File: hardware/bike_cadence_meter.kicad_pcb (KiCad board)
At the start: 2 copper layers, 43.5 x 29 mm, 16 parts, among them J1 3034, J2 1x04, SW1 SW_Push, U2 LSM6DS3, Y1 CM130_9pf_+-20ppm

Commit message: Add manufacturing files
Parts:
- added GND: TestPoint, TestPoint:TestPoint_Pad_D1.0mm, F.Cu at (36.2, 43.8)
- added P13: TestPoint, TestPoint:TestPoint_Pad_D1.0mm, F.Cu at (51.8, 36.2)
- added TP4: TestPoint, TestPoint:TestPoint_Pad_D1.0mm, F.Cu at (57.2, 30.8)
- added VCC: TestPoint, TestPoint:TestPoint_Pad_D1.0mm, F.Cu at (26.5, 43.8)
- moved J2 0.79 mm to (28.6, 46.8)
- moved C1 0.24 mm to (51.0, 28.0)
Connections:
- U1 pad 13: unconnected-(U1-I/O-Pad13) -> Net-(TP1-Pad1)
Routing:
- net Net-(TP1-Pad1): track 0.00 -> 3.81 mm
- net GND: track 55.0 -> 56.3 mm
- net VCC: track 108.6 -> 109.3 mm
- net SWDIO: track 25.6 -> 26.1 mm
- net SWDCLK: track 23.9 -> 24.5 mm

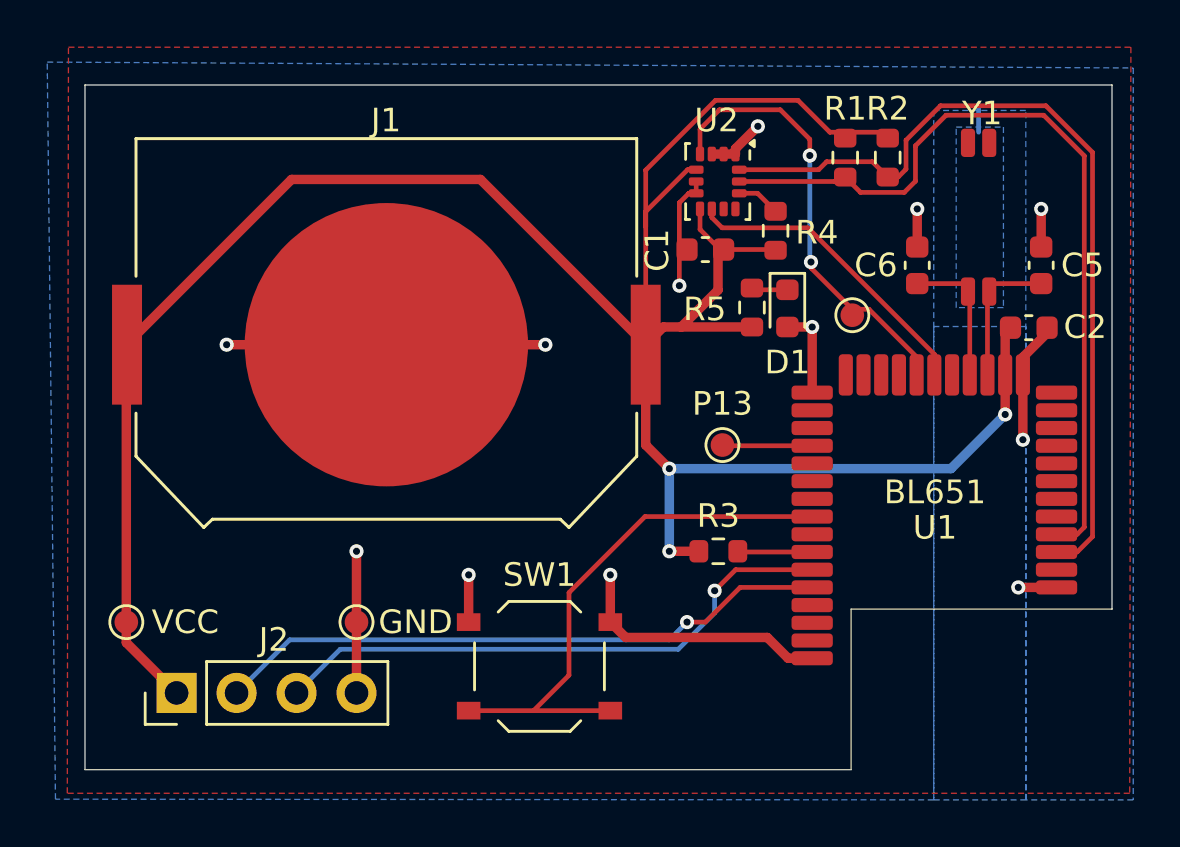
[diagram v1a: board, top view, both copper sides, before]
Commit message: Fixed reversed LED
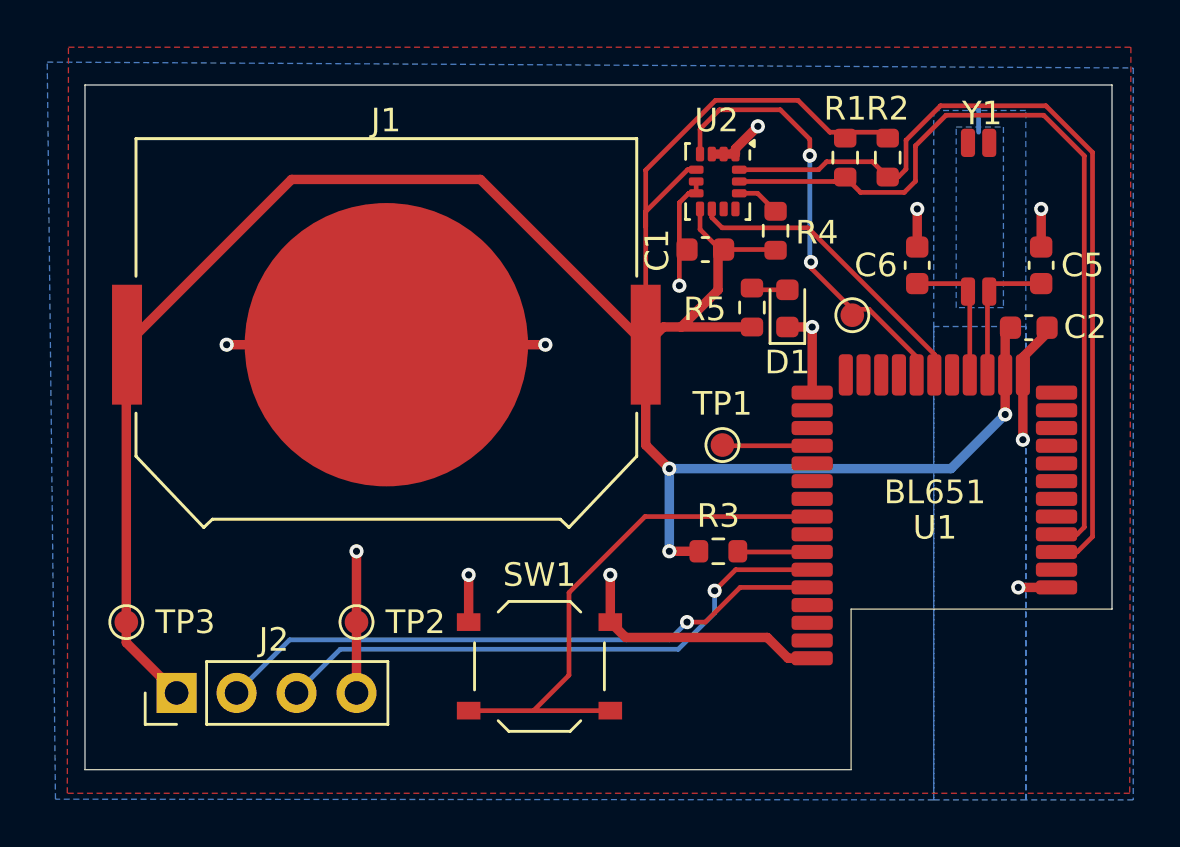
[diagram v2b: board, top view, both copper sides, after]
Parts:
- turned D1 to 90 degrees
- renumbered P13 to TP1, GND to TP2, VCC to TP3
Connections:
- D1 pad 1: Net-(D1-K) -> GND
- D1 pad 2: GND -> Net-(D1-A)
- R5 pad 2: Net-(D1-K) -> Net-(D1-A)
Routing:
- net Net-(D1-K): track 1.64 -> 0.00 mm
- net Net-(D1-A): track 0.00 -> 1.64 mm
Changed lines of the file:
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@@
 	(net 36 "unconnected-(U2-NC-Pad11)")
 	(net 37 "unconnected-(U2-NC-Pad10)")
-	(net 38 "Net-(D1-K)")
+	(net 38 "Net-(D1-A)")
 	(net 39 "Net-(U2-CS)")
 	(net 40 "I{slash}O 9")
@@
 			)
 		)
+		(property "JLPCB #" " C22775"
+			(at 0 0 90)
+			(unlocked yes)
+			(layer "F.Fab")
+			(hide yes)
+			(effects
+				(font
+					(size 1 1)
+					(thickness 0.15)
+				)
+			)
+		)
 		(property ki_fp_filters "R_*")
 		(sheetname "Root")
@@
 			(layers "F.Cu" "F.Paste" "F.Mask")
 			(roundrect_rratio 0.25)
-			(net 38 "Net-(D1-K)")
+			(net 38 "Net-(D1-A)")
 			(pintype "passive")
 		)
@@
 			)
 		)
+		(property "JLPCB #" " C23162"
+			(at 0 0 90)
+			(unlocked yes)
+			(layer "F.Fab")
+			(hide yes)
+			(effects
+				(font
+					(size 1 1)
+					(thickness 0.15)
+				)
+			)
+		)
 		(property ki_fp_filters "R_*")
 		(sheetname "Root")
@@
 			)
 		)
+		(property "JLPCB #" " C23162"
+			(at 0 0 -90)
+			(unlocked yes)
+			(layer "F.Fab")
+			(hide yes)
+			(effects
+				(font
+					(size 1 1)
+					(thickness 0.15)
+				)
+			)
+		)
 		(property ki_fp_filters "R_*")
 		(sheetname "Root")
@@
 		(descr "SMD pad as test Point, diameter 1.0mm")
 		(tags "test point SMD pad")
-		(property "Reference" "P13"
+		(property "Reference" "TP1"
 			(at 0 -1.75 0)
 			(layer "F.SilkS")
@@
 			)
 		)
+		(property "JLPCB #" " C23162"
+			(at 0 0 -90)
+			(unlocked yes)
+			(layer "F.Fab")
+			(hide yes)
+			(effects
+				(font
+					(size 1 1)
+					(thickness 0.15)
+				)
+			)
+		)
 		(property ki_fp_filters "R_*")
 		(sheetname "Root")
@@
 			)
 		)
+		(property "JLPCB #" " C14663"
+			(at 0 0 180)
+			(unlocked yes)
+			(layer "F.Fab")
+			(hide yes)
+			(effects
+				(font
+					(size 1 1)
+					(thickness 0.15)
+				)
+			)
+		)
 		(property ki_fp_filters "C_*")
 		(sheetname "Root")
@@
 			)
 		)
+		(property "JLPCB #" " C38523"
+			(at 0 0 -90)
+			(unlocked yes)
+			(layer "F.Fab")
+			(hide yes)
+			(effects
+				(font
+					(size 1 1)
+					(thickness 0.15)
+				)
+			)
+		)
 		(property ki_fp_filters "C_*")
 		(sheetname "Root")
@@
 			)
 		)
+		(property "JLPCB #" " C14663"
+			(at 0 0 180)
+			(unlocked yes)
+			(layer "F.Fab")
+			(hide yes)
+			(effects
+				(font
+					(size 1 1)
+					(thickness 0.15)
+				)
+			)
+		)
 		(property ki_fp_filters "C_*")
 		(sheetname "Root")
@@
 			)
 		)
+		(property "LCSC" " C23162"
+			(at 0 0 0)
+			(unlocked yes)
+			(layer "F.Fab")
+			(hide yes)
+			(effects
+				(font
+					(size 1 1)
+					(thickness 0.15)
+				)
+			)
+		)
+		(property "JLPCB #" " C23162"
+			(at 0 0 0)
+			(unlocked yes)
+			(layer "F.Fab")
+			(hide yes)
+			(effects
+				(font
+					(size 1 1)
+					(thickness 0.15)
+				)
+			)
+		)
 		(property ki_fp_filters "R_*")
 		(sheetname "Root")
@@
 		(descr "SMD pad as test Point, diameter 1.0mm")
 		(tags "test point SMD pad")
-		(property "Reference" "VCC"
+		(property "Reference" "TP3"
 			(at 2.5 0 0)
 			(layer "F.SilkS")
@@
 			)
 		)
+		(property "JLPCB #" " C318884"
+			(at 0 0 180)
+			(unlocked yes)
+			(layer "F.Fab")
+			(hide yes)
+			(effects
+				(font
+					(size 1 1)
+					(thickness 0.15)
+				)
+			)
+		)
 		(sheetname "Root")
 		(sheetfile "bike_cadence_meter.kicad_sch")
@@
 	(footprint "LED_SMD:LED_0603_1608Metric"
 		(layer "F.Cu")
-		(at 54.5 30.4625 -90)
+		(at 54.5 30.4625 90)
 		(descr "LED SMD 0603 (1608 Metric), square (rectangular) end terminal, IPC_7351 nominal, (Body size source: http://www.tortai-tech.com/upload/download/2011102023233369053.pdf), generated with kicad-footprint-generator")
 		(tags "LED")
 		(property "Reference" "D1"
-			(at 2.2875 0 180)
+			(at -2.2875 0 360)
 			(layer "F.SilkS")
 			(effects
@@
 		)
 		(property "Footprint" "LED_SMD:LED_0603_1608Metric"
-			(at 0 0 -90)
+			(at 0 0 90)
 			(unlocked yes)
 			(layer "F.Fab")
@@
 		)
 		(property "Datasheet" ""
-			(at 0 0 -90)
+			(at 0 0 90)
 			(unlocked yes)
 			(layer "F.Fab")
@@
 		)
 		(property "Description" "Light emitting diode"
-			(at 0 0 -90)
+			(at 0 0 90)
 			(unlocked yes)
 			(layer "F.Fab")
@@
 			)
 		)
+		(property "JLPCB #" "C2286"
+			(at 0 0 90)
+			(unlocked yes)
+			(layer "F.Fab")
+			(hide yes)
+			(effects
+				(font
+					(size 1 1)
+					(thickness 0.15)
+				)
+			)
+		)
 		(property ki_fp_filters "LED* LED_SMD:* LED_THT:*")
 		(sheetname "Root")
@@
 		(attr smd)
 		(fp_line
-			(start -1.485 0.735)
-			(end 0.8 0.735)
+			(start 0.8 -0.735)
+			(end -1.485 -0.735)
 			(stroke
 				(width 0.12)
@@
 		)
 		(fp_line
-			(start 0.8 -0.735)
-			(end -1.485 -0.735)
+			(start -1.485 0.735)
+			(end 0.8 0.735)
 			(stroke
 				(width 0.12)
@@
 		)
 		(fp_line
-			(start -1.48 0.73)
-			(end -1.48 -0.73)
+			(start 1.48 -0.73)
+			(end 1.48 0.73)
 			(stroke
 				(width 0.05)
@@
 		)
 		(fp_line
-			(start 1.48 0.73)
-			(end -1.48 0.73)
+			(start -1.48 -0.73)
+			(end 1.48 -0.73)
 			(stroke
 				(width 0.05)
@@
 		)
 		(fp_line
-			(start -1.48 -0.73)
-			(end 1.48 -0.73)
+			(start 1.48 0.73)
+			(end -1.48 0.73)
 			(stroke
 				(width 0.05)
@@
 		)
 		(fp_line
-			(start 1.48 -0.73)
-			(end 1.48 0.73)
+			(start -1.48 0.73)
+			(end -1.48 -0.73)
 			(stroke
 				(width 0.05)
@@
 		)
 		(fp_line
-			(start -0.8 0.4)
-			(end 0.8 0.4)
+			(start 0.8 -0.4)
+			(end -0.5 -0.4)
 			(stroke
 				(width 0.1)
@@
 		)
 		(fp_line
-			(start 0.8 0.4)
-			(end 0.8 -0.4)
+			(start -0.5 -0.4)
+			(end -0.8 -0.1)
 			(stroke
 				(width 0.1)
@@
 		)
 		(fp_line
-			(start -0.5 -0.4)
-			(end -0.8 -0.1)
+			(start 0.8 0.4)
+			(end 0.8 -0.4)
 			(stroke
 				(width 0.1)
@@
 		)
 		(fp_line
-			(start 0.8 -0.4)
-			(end -0.5 -0.4)
+			(start -0.8 0.4)
+			(end 0.8 0.4)
 			(stroke
 				(width 0.1)
@@
 		)
 		(pad "1" smd roundrect
-			(at -0.7875 0 270)
+			(at -0.7875 0 90)
 			(size 0.875 0.95)
 			(layers "F.Cu" "F.Paste" "F.Mask")
 			(roundrect_rratio 0.25)
-			(net 38 "Net-(D1-K)")
+			(net 1 "GND")
 			(pinfunction "K")
 			(pintype "passive")
 		)
 		(pad "2" smd roundrect
-			(at 0.7875 0 270)
+			(at 0.7875 0 90)
 			(size 0.875 0.95)
 			(layers "F.Cu" "F.Paste" "F.Mask")
 			(roundrect_rratio 0.25)
-			(net 1 "GND")
+			(net 38 "Net-(D1-A)")
 			(pinfunction "A")
 			(pintype "passive")
@@
 			)
 		)
+		(property "JLPCB #" " C38523"
+			(at 0 0 -90)
+			(unlocked yes)
+			(layer "F.Fab")
+			(hide yes)
+			(effects
+				(font
+					(size 1 1)
+					(thickness 0.15)
+				)
+			)
+		)
 		(property ki_fp_filters "C_*")
 		(sheetname "Root")
@@
 			)
 		)
+		(property "JLPCB #" " C967633"
+			(at 0 0 -90)
+			(unlocked yes)
+			(layer "F.Fab")
+			(hide yes)
+			(effects
+				(font
+					(size 1 1)
+					(thickness 0.15)
+				)
+			)
+		)
 		(property ki_fp_filters "LGA*3x2.5mm*P0.5mm*LayoutBorder3x4y*")
 		(sheetname "Root")
@@
 		(descr "SMD pad as test Point, diameter 1.0mm")
 		(tags "test point SMD pad")
-		(property "Reference" "GND"
+		(property "Reference" "TP2"
 			(at 2.5 0 180)
 			(layer "F.SilkS")
